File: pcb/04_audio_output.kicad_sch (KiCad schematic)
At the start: 4 parts, among them CN2 HEADPHONE 3.5mm

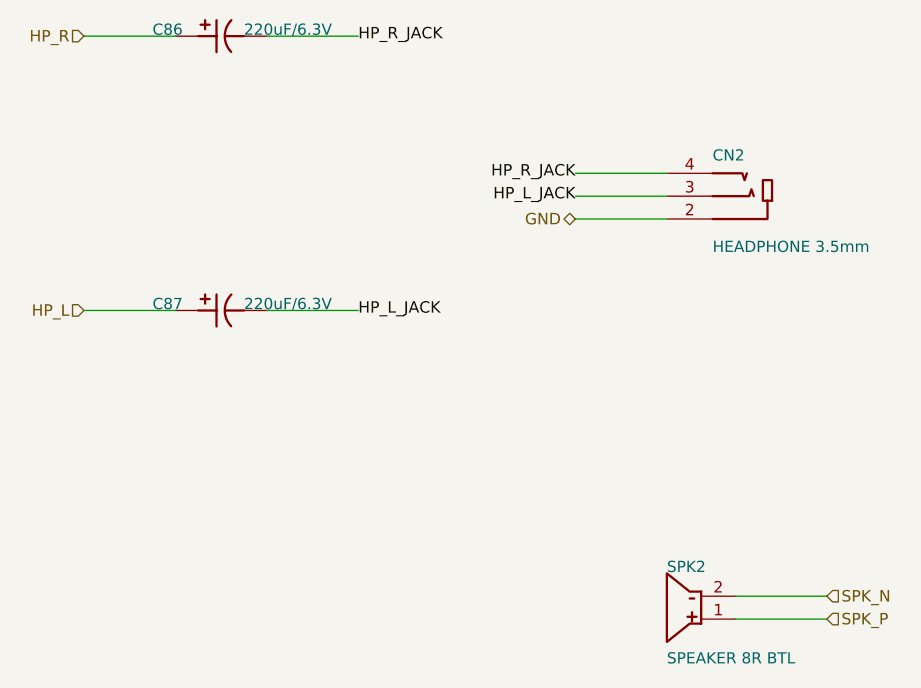
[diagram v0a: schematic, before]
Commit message: 修复原理图电源网络并更新项目文档
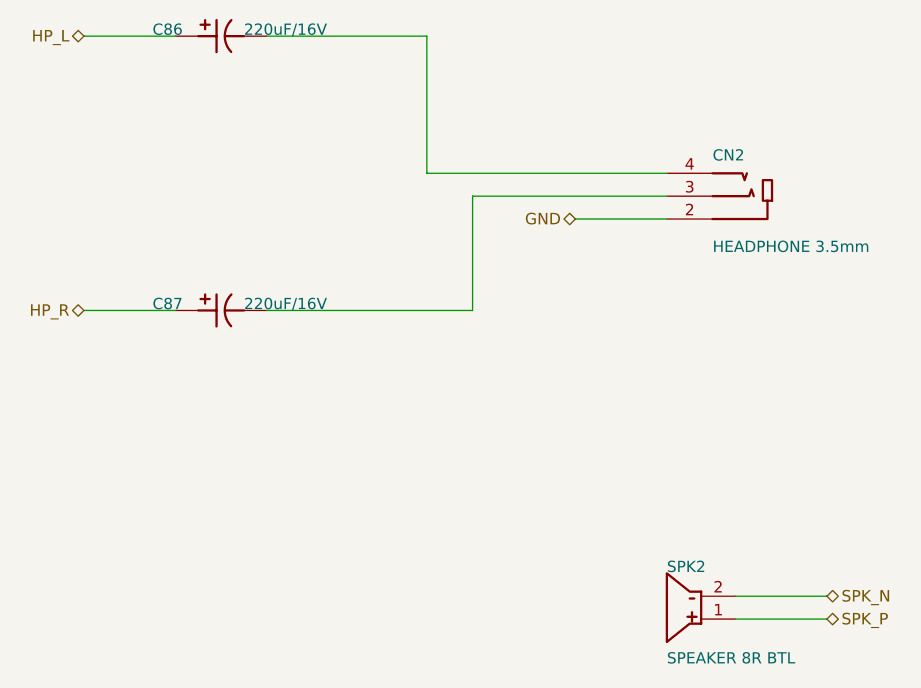
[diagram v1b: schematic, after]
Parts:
- C86, C87: value 220uF/6.3V -> 220uF/16V
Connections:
- net HP_L: now also C86.1; no longer C87.1
- net HP_R: now also C87.1; no longer C86.1
- net HP_L_JACK: no longer names the net of C87.2, CN2.3
- net HP_R_JACK: no longer names the net of C86.2, CN2.4
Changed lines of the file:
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@@
 	(wire
 		(pts
-			(xy 95.25 100.33) (xy 105.41 100.33)
+			(xy 74.93 69.85) (xy 85.09 69.85)
 		)
 		(stroke
@@
 	(wire
 		(pts
-			(xy 139.7 87.63) (xy 129.54 87.63)
-		)
-		(stroke
-			(width 0)
-			(type default)
-		)
-	)
-	(wire
-		(pts
-			(xy 85.09 69.85) (xy 74.93 69.85)
-		)
-		(stroke
-			(width 0)
-			(type default)
-		)
-	)
-	(wire
-		(pts
 			(xy 147.32 134.62) (xy 157.48 134.62)
 		)
@@
 	(wire
 		(pts
-			(xy 85.09 100.33) (xy 74.93 100.33)
-		)
-		(stroke
-			(width 0)
-			(type default)
-		)
-	)
-	(wire
-		(pts
-			(xy 139.7 85.09) (xy 129.54 85.09)
-		)
-		(stroke
-			(width 0)
-			(type default)
-		)
-	)
-	(wire
-		(pts
-			(xy 139.7 90.17) (xy 129.54 90.17)
-		)
-		(stroke
-			(width 0)
-			(type default)
-		)
-	)
-	(wire
-		(pts
-			(xy 95.25 69.85) (xy 105.41 69.85)
-		)
-		(stroke
-			(width 0)
-			(type default)
-		)
-	)
-	(label "HP_L_JACK"
-		(at 129.54 87.63 180)
+			(xy 118.11 100.33) (xy 118.11 87.63)
+		)
+		(stroke
+			(width 0)
+			(type default)
+		)
+	)
+	(wire
+		(pts
+			(xy 118.11 87.63) (xy 139.7 87.63)
+		)
+		(stroke
+			(width 0)
+			(type default)
+		)
+	)
+	(wire
+		(pts
+			(xy 95.25 100.33) (xy 118.11 100.33)
+		)
+		(stroke
+			(width 0)
+			(type default)
+		)
+	)
+	(wire
+		(pts
+			(xy 129.54 90.17) (xy 139.7 90.17)
+		)
+		(stroke
+			(width 0)
+			(type default)
+		)
+	)
+	(wire
+		(pts
+			(xy 74.93 100.33) (xy 85.09 100.33)
+		)
+		(stroke
+			(width 0)
+			(type default)
+		)
+	)
+	(wire
+		(pts
+			(xy 113.03 85.09) (xy 139.7 85.09)
+		)
+		(stroke
+			(width 0)
+			(type default)
+		)
+	)
+	(wire
+		(pts
+			(xy 113.03 69.85) (xy 113.03 85.09)
+		)
+		(stroke
+			(width 0)
+			(type default)
+		)
+	)
+	(wire
+		(pts
+			(xy 95.25 69.85) (xy 113.03 69.85)
+		)
+		(stroke
+			(width 0)
+			(type default)
+		)
+	)
+	(hierarchical_label "SPK_N"
+		(shape bidirectional)
+		(at 157.48 132.08 0)
 		(effects
 			(font
 				(size 1.27 1.27)
 			)
-			(justify right)
-		)
-	)
-	(label "HP_R_JACK"
-		(at 129.54 85.09 180)
-		(effects
-			(font
-				(size 1.27 1.27)
-			)
-			(justify right)
-		)
-	)
-	(label "HP_R_JACK"
-		(at 105.41 69.85 0)
-		(effects
-			(font
-				(size 1.27 1.27)
-			)
 			(justify left)
 		)
 	)
-	(label "HP_L_JACK"
-		(at 105.41 100.33 0)
-		(effects
-			(font
-				(size 1.27 1.27)
-			)
-			(justify left)
-		)
-	)
-	(hierarchical_label "HP_R"
-		(shape input)
+	(hierarchical_label "HP_L"
+		(shape bidirectional)
 		(at 74.93 69.85 180)
 		(effects
@@
 	)
 	(hierarchical_label "SPK_P"
-		(shape input)
+		(shape bidirectional)
 		(at 157.48 134.62 0)
 		(effects
@@
 		)
 	)
-	(hierarchical_label "HP_L"
-		(shape input)
+	(hierarchical_label "HP_R"
+		(shape bidirectional)
 		(at 74.93 100.33 180)
 		(effects
@@
 			)
 			(justify right)
-		)
-	)
-	(hierarchical_label "SPK_N"
-		(shape input)
-		(at 157.48 132.08 0)
-		(effects
-			(font
-				(size 1.27 1.27)
-			)
-			(justify left)
 		)
 	)
@@
 			)
 		)
-		(property "Value" "220uF/6.3V"
+		(property "Value" "220uF/16V"
 			(at 92.71 100.33 0)
 			(show_name no)
@@
 			)
 		)
-		(property "Value" "220uF/6.3V"
+		(property "Value" "220uF/16V"
 			(at 92.71 69.85 0)
 			(show_name no)
